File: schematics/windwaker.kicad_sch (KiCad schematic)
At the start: 4 parts, among them SW1 SW_Push, U1 WEMOS_C3_mini, U2 This should be a tft later

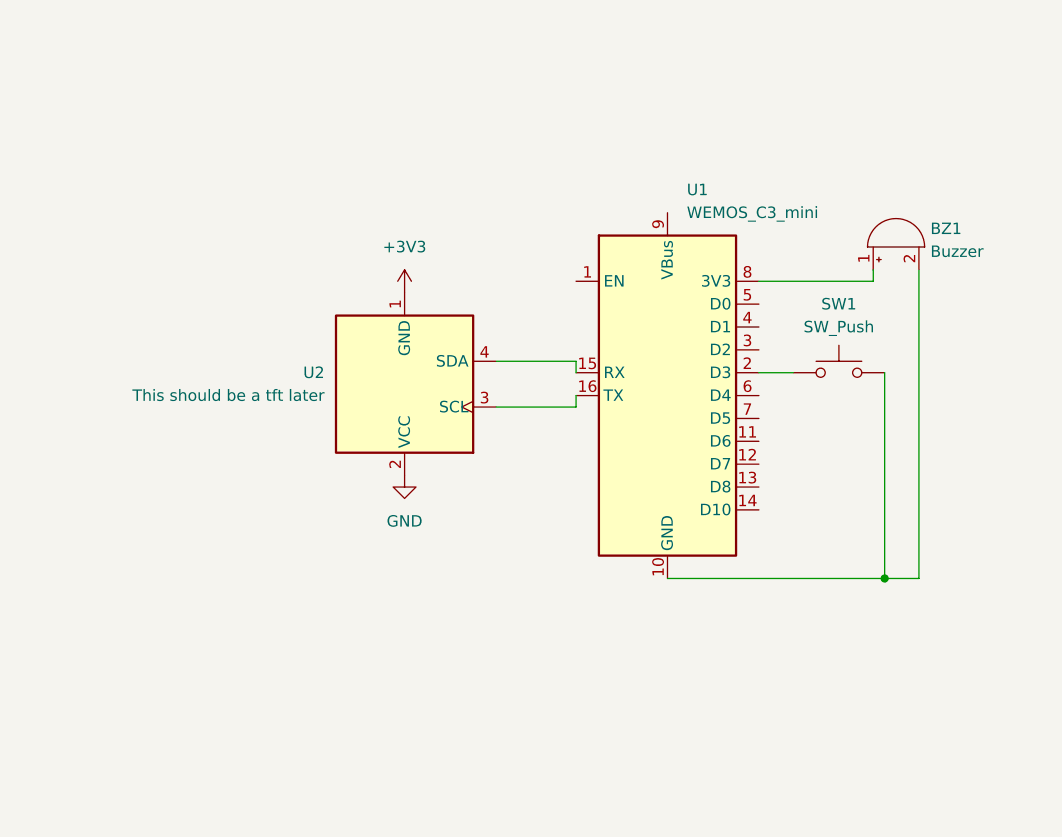
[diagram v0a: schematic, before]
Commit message: wow, a rough sketch, and a real footprint!
rough sketch by me and footprint for the thing. basic routing can happen now
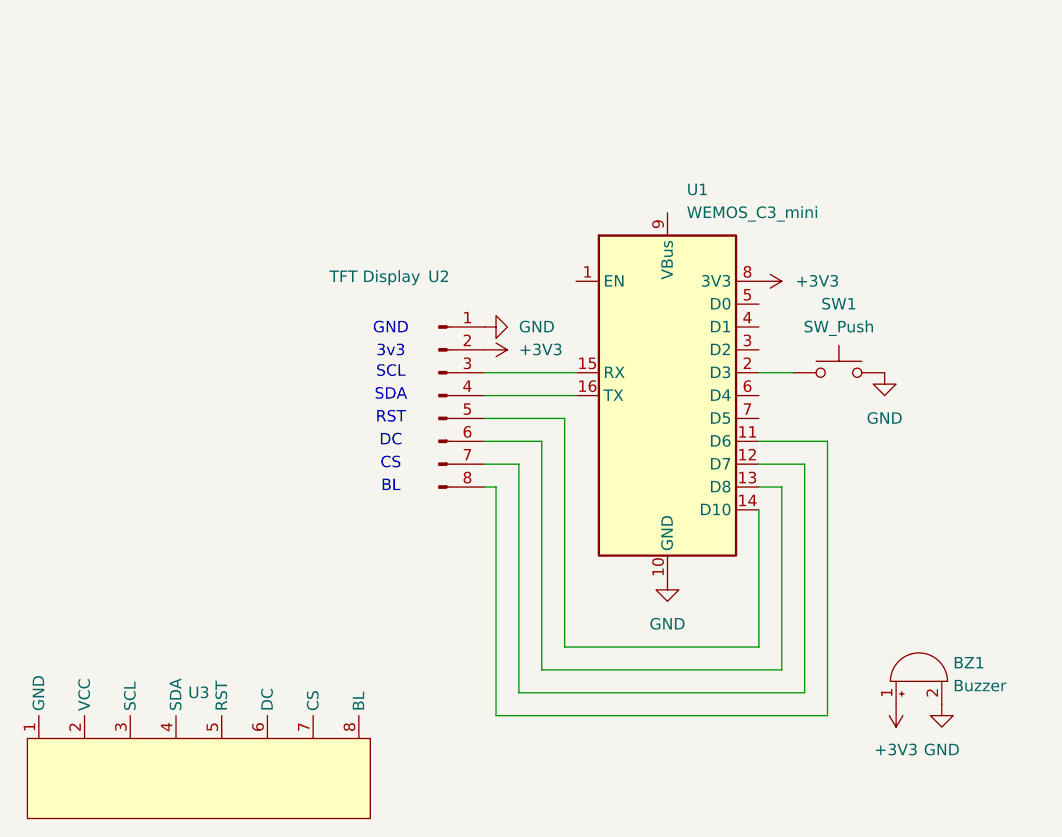
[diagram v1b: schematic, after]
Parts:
- removed U2: This should be a tft later, Display:ER_OLEDM0.91_1x-I2C, symbol Display_Graphic:ER_OLEDM0.91_1x-I2C
- added U2: TFT Display, my_custom_library:TFT-Display_ST7789_2.25in_76x284_8P, symbol Connector:Conn_01x08_Pin
- added U3: (no value), symbol my_custom_symbollib:TFT-display
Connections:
- net +3V3: now also BZ1.1 (+), U1.8 (3V3), U2.2 (Pin_2)
- net GND: now also BZ1.2 (-), SW1.2, U1.10 (GND), U2.1 (Pin_1)
- net at U1.11 (D6): now also U2.8 (Pin_8)
- net at U1.12 (D7): now also U2.7 (Pin_7)
- net at U1.13 (D8): now also U2.6 (Pin_6)
- net at U1.14 (D10): now also U2.5 (Pin_5)
- net at U1.15 (RX): now also U2.3 (Pin_3)
- net at U1.16 (TX): now also U2.4 (Pin_4)
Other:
- note added: "3v3"
- note added: "BL"
- note added: "CS"
- note added: "DC"
- note added: "GND"
- note added: "RST"
- note added: "SCL"
- note added: "SDA"
- moved on the sheet: BZ1

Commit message: adding some 3d models and routing the pcb
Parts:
- removed U3: (no value), symbol my_custom_symbollib:TFT-display
- added SW2, SW3, SW4: SW_Push, Button_Switch_Keyboard:SW_Cherry_MX_1.00u_PCB, symbol Switch:SW_Push
- BZ1: footprint (none) -> my_custom_library:Buzzer_12x9.5RM7.6
- SW1: footprint (none) -> Button_Switch_Keyboard:SW_Cherry_MX_1.00u_PCB
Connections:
- net GND: now also SW2.2, SW3.2, SW4.2
- net at U1.3 (D2): now also SW2.1
- net at U1.4 (D1): now also SW3.1
- net at U1.5 (D0): now also SW4.1
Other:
- moved on the sheet: BZ1, SW1

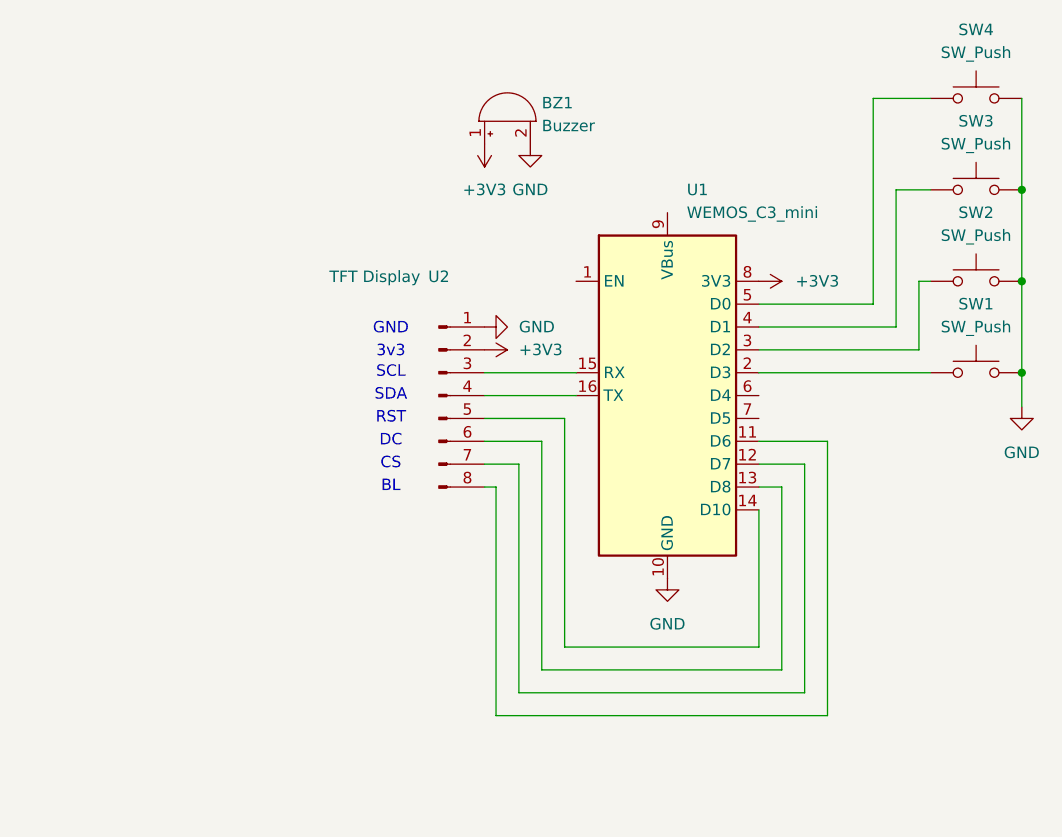
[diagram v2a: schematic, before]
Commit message: fixed pcb and firmware
buzz should've been with pin
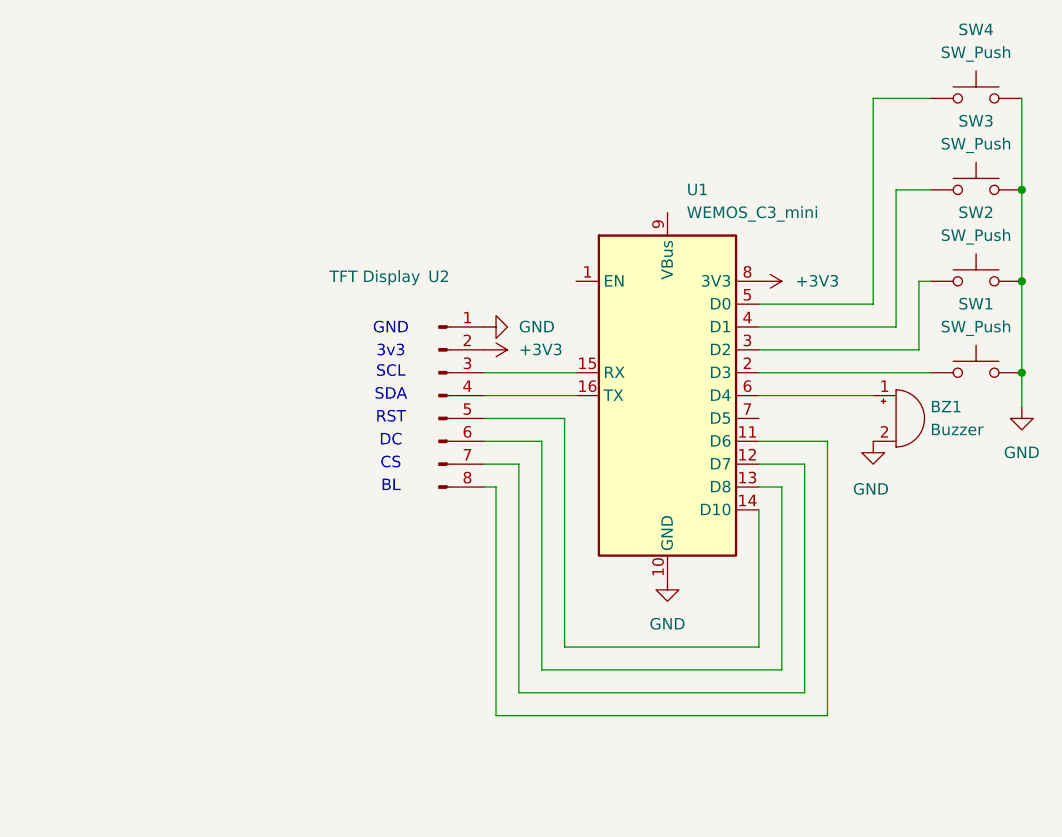
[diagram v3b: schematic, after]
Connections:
- net +3V3: no longer BZ1.1 (+)
- net at U1.6 (D4): now also BZ1.1 (+)
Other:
- moved on the sheet: BZ1
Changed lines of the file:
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@@
+	(wire
+		(pts
+			(xy 161.29 92.71) (xy 173.99 92.71)
+		)
+		(stroke
+			(width 0)
+			(type default)
+		)
+	)
 	(wire
 		(pts
@@
 	)
 	(symbol
-		(lib_id "power:+3V3")
-		(at 130.81 64.77 180)
-		(unit 1)
-		(body_style 1)
-		(exclude_from_sim no)
-		(in_bom yes)
-		(on_board yes)
-		(in_pos_files yes)
-		(dnp no)
-		(fields_autoplaced yes)
-		(property "Reference" "#PWR07"
-			(at 130.81 60.96 0)
-			(hide yes)
-			(show_name no)
-			(do_not_autoplace no)
-			(effects
-				(font
-					(size 1.27 1.27)
-				)
-			)
-		)
-		(property "Value" "+3V3"
-			(at 130.81 69.85 0)
-			(show_name no)
-			(do_not_autoplace no)
-			(effects
-				(font
-					(size 1.27 1.27)
-				)
-			)
-		)
-		(property "Footprint" ""
-			(at 130.81 64.77 0)
-			(hide yes)
-			(show_name no)
-			(do_not_autoplace no)
-			(effects
-				(font
-					(size 1.27 1.27)
-				)
-			)
-		)
-		(property "Datasheet" ""
-			(at 130.81 64.77 0)
-			(hide yes)
-			(show_name no)
-			(do_not_autoplace no)
-			(effects
-				(font
-					(size 1.27 1.27)
-				)
-			)
-		)
-		(property "Description" "Power symbol creates a global label with name \"+3V3\""
-			(at 130.81 64.77 0)
-			(hide yes)
-			(show_name no)
-			(do_not_autoplace no)
-			(effects
-				(font
-					(size 1.27 1.27)
-				)
-			)
-		)
-		(pin "1"
-		)
-		(instances
-			(project "windwaker"
-				(path "/02a39cfe-b783-40f3-817f-4ab00e2c0b53"
-					(reference "#PWR07")
-					(unit 1)
-				)
-			)
-		)
-	)
-	(symbol
 		(lib_id "Device:Buzzer")
-		(at 133.35 62.23 90)
+		(at 176.53 95.25 0)
 		(unit 1)
 		(body_style 1)
@@
 		(fields_autoplaced yes)
 		(property "Reference" "BZ1"
-			(at 137.16 60.2048 90)
-			(show_name no)
-			(do_not_autoplace no)
-			(effects
-				(font
-					(size 1.27 1.27)
-				)
-				(justify right)
+			(at 180.34 93.9799 0)
+			(show_name no)
+			(do_not_autoplace no)
+			(effects
+				(font
+					(size 1.27 1.27)
+				)
+				(justify left)
 			)
 		)
 		(property "Value" "Buzzer"
-			(at 137.16 62.7448 90)
-			(show_name no)
-			(do_not_autoplace no)
-			(effects
-				(font
-					(size 1.27 1.27)
-				)
-				(justify right)
+			(at 180.34 96.5199 0)
+			(show_name no)
+			(do_not_autoplace no)
+			(effects
+				(font
+					(size 1.27 1.27)
+				)
+				(justify left)
 			)
 		)
 		(property "Footprint" "my_custom_library:Buzzer_12x9.5RM7.6"
-			(at 130.81 62.865 90)
+			(at 175.895 92.71 90)
 			(hide yes)
 			(show_name no)
@@
 		)
 		(property "Datasheet" ""
-			(at 130.81 62.865 90)
+			(at 175.895 92.71 90)
 			(hide yes)
 			(show_name no)
@@
 		)
 		(property "Description" "Buzzer, polarized"
-			(at 133.35 62.23 0)
+			(at 176.53 95.25 0)
 			(hide yes)
 			(show_name no)
@@
 	(symbol
 		(lib_id "power:GND")
-		(at 135.89 64.77 0)
+		(at 173.99 97.79 0)
 		(unit 1)
 		(body_style 1)
@@
 		(in_pos_files yes)
 		(dnp no)
-		(fields_autoplaced yes)
 		(property "Reference" "#PWR08"
-			(at 135.89 71.12 0)
+			(at 173.99 104.14 0)
 			(hide yes)
 			(show_name no)
@@
 		)
 		(property "Value" "GND"
-			(at 135.89 69.85 0)
+			(at 173.736 103.124 0)
 			(show_name no)
 			(do_not_autoplace no)
@@
 		)
 		(property "Footprint" ""
-			(at 135.89 64.77 0)
+			(at 173.99 97.79 0)
 			(hide yes)
 			(show_name no)
@@
 		)
 		(property "Datasheet" ""
-			(at 135.89 64.77 0)
+			(at 173.99 97.79 0)
 			(hide yes)
 			(show_name no)
@@
 		)
 		(property "Description" "Power symbol creates a global label with name \"GND\" , ground"
-			(at 135.89 64.77 0)
-			(hide yes)
-			(show_name no)
+			(at 173.99 97.79 0)
+			(hide yes)
+			(show_name no)
